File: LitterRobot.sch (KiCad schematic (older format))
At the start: 1 part, among them J1 Conn_02x02_Odd_Even

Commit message: Added Hirose footprints
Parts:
- removed J1: Conn_02x02_Odd_Even, LitterRobot:Hirose_DF11C-4DP-2V(57), symbol Connector_Generic:Conn_02x02_Odd_Even
- added J1: DF11C-4DP-2V(57), LitterRobot:Hirose_DF11C-4DP-2V(57), symbol Connector_Generic_MountingPin:Conn_02x02_Odd_Even_MountingPin
- added J2: Hirose_DF11C-6DP-2V(57), LitterRobot:Hirose_DF11C-6DP-2V(57), symbol Connector_Generic_MountingPin:Conn_02x03_Odd_Even_MountingPin
- added J3: DF11C-8DP-2V(57), LitterRobot:Hirose_DF11C-8DP-2V(57), symbol Connector_Generic_MountingPin:Conn_02x04_Odd_Even_MountingPin
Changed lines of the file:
@@
 encoding utf-8
 Sheet 1 1
-Title "Litter robot 3 - Main board"
+Title "Litter Robot 3 - Main board"
 Date "2021-02-27"
 Rev "A1"
@@
 $EndDescr
 $Comp
-L Connector_Generic:Conn_02x02_Odd_Even J1
-U 1 1 603B33C5
-P 2000 2050
-F 0 "J1" H 2050 2267 50  0000 C CNN
-F 1 "Conn_02x02_Odd_Even" H 2050 2176 50  0000 C CNN
-F 2 "LitterRobot:Hirose_DF11C-4DP-2V(57)" H 2000 2050 50  0001 C CNN
-F 3 "https://www.hirose.com/en/product/document?clcode=CL0543-0682-1-57&productname=DF11C-4DP-2V(57)&series=DF11&documenttype=2DDrawing&lang=en&documentid=0000926110" H 2000 2050 50  0001 C CNN
-	1    2000 2050
+L Connector_Generic_MountingPin:Conn_02x02_Odd_Even_MountingPin J1
+U 1 1 603B9D61
+P 2050 1550
+F 0 "J1" H 2100 1767 50  0000 C CNN
+F 1 "DF11C-4DP-2V(57)" H 2100 1676 50  0000 C CNN
+F 2 "LitterRobot:Hirose_DF11C-4DP-2V(57)" H 2050 1550 50  0001 C CNN
+F 3 "https://www.hirose.com/en/product/document?clcode=CL0543-0682-1-57&productname=DF11C-4DP-2V(57)&series=DF11&documenttype=2DDrawing&lang=en&documentid=0000926110" H 2050 1550 50  0001 C CNN
+	1    2050 1550
 	1    0    0    -1
 $EndComp
+$Comp
+L Connector_Generic_MountingPin:Conn_02x03_Odd_Even_MountingPin J2
+U 1 1 603BB210
+P 2050 2650
+F 0 "J2" H 2100 2967 50  0000 C CNN
+F 1 "Hirose_DF11C-6DP-2V(57)" H 2100 2876 50  0000 C CNN
+F 2 "LitterRobot:Hirose_DF11C-6DP-2V(57)" H 2050 2650 50  0001 C CNN
+F 3 "https://www.hirose.com/en/product/document?clcode=CL0543-0683-4-57&productname=DF11C-6DP-2V(57)&series=DF11&documenttype=2DDrawing&lang=en&documentid=0000926113" H 2050 2650 50  0001 C CNN
+	1    2050 2650
+	1    0    0    -1
+$EndComp
+$Comp
+L Connector_Generic_MountingPin:Conn_02x04_Odd_Even_MountingPin J3
+U 1 1 603BC30E
+P 2050 3650
+F 0 "J3" H 2100 3967 50  0000 C CNN
+F 1 "DF11C-8DP-2V(57)" H 2100 3876 50  0000 C CNN
+F 2 "LitterRobot:Hirose_DF11C-8DP-2V(57)" H 2050 3650 50  0001 C CNN
+F 3 "https://www.hirose.com/en/product/document?clcode=CL0543-0684-7-57&productname=DF11C-8DP-2V(57)&series=DF11&documenttype=2DDrawing&lang=en&documentid=0000999153" H 2050 3650 50  0001 C CNN
+	1    2050 3650
+	1    0    0    -1
+$EndComp

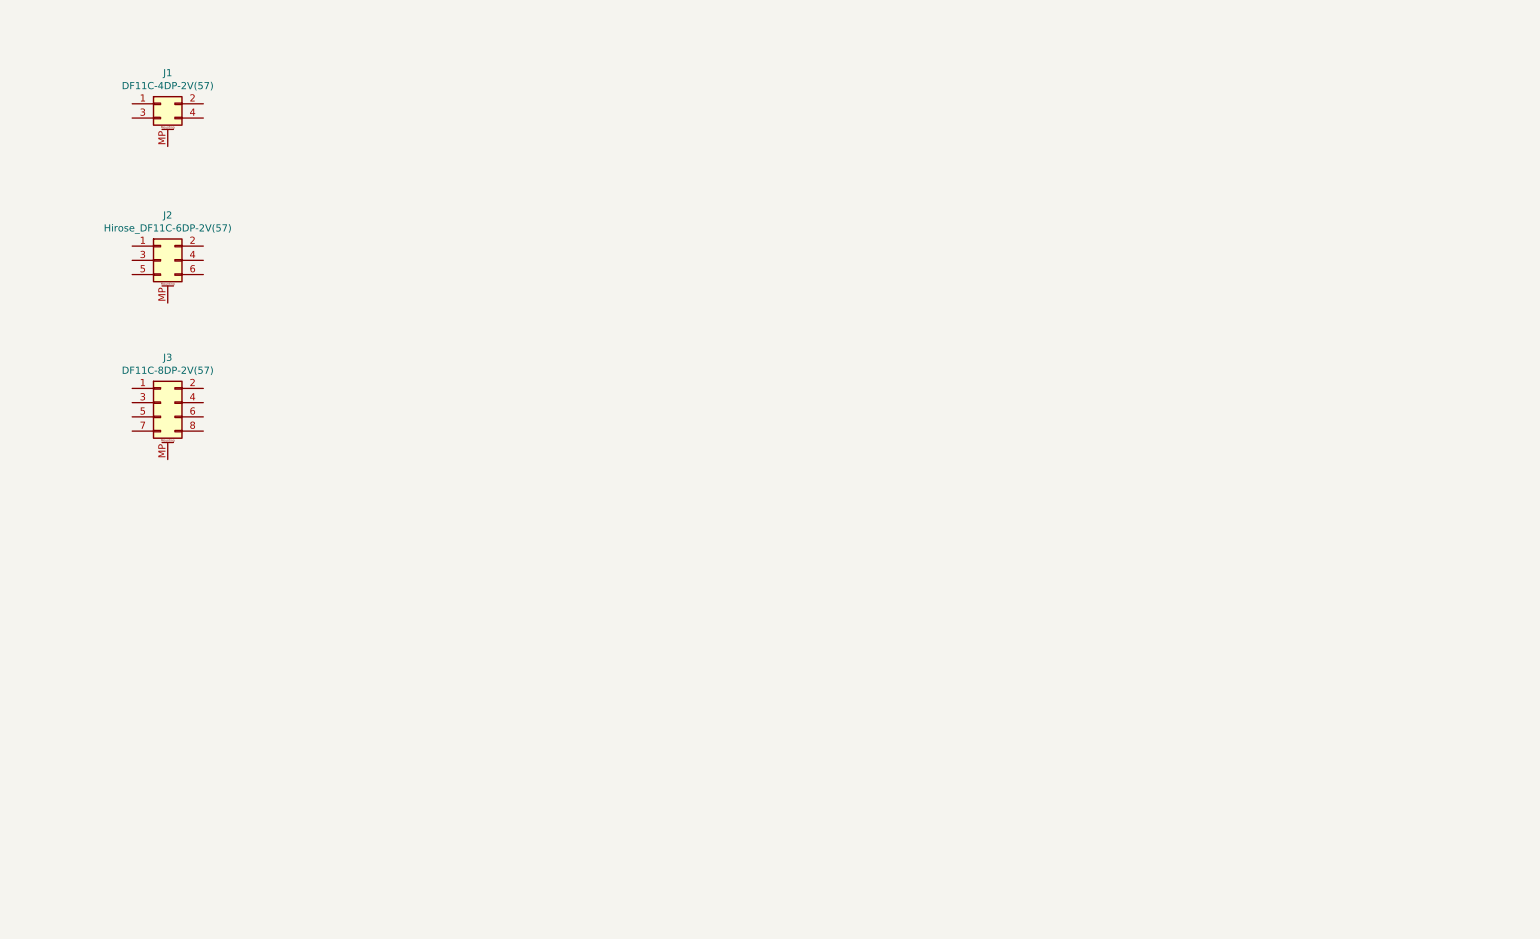
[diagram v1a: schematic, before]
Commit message: Add RGB LEDs to the schematic
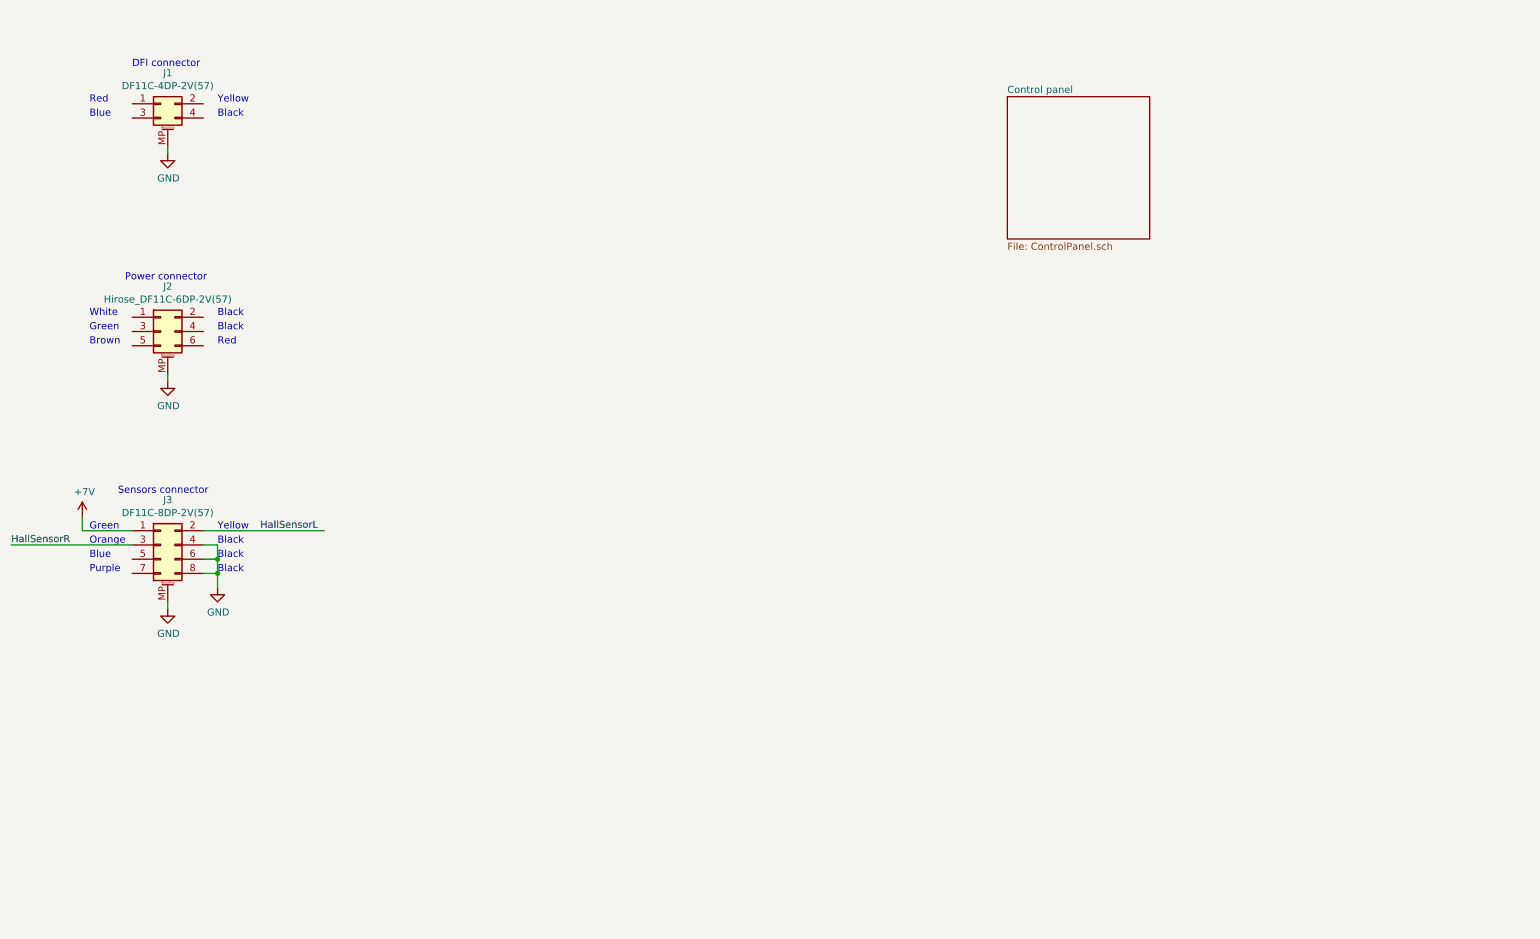
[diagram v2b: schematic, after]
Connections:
- net labels added: +7V, GND, HallSensorL, HallSensorR
- wire segments 0 -> 13
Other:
- note added: "Black"
- note added: "Blue"
- note added: "Brown"
- note added: "DFI connector"
- note added: "Green"
- note added: "Orange"
- note added: "Power connector"
- note added: "Purple"
- note added: "Red"
- note added: "Sensors connector"
- note added: "White"
- note added: "Yellow"
- moved on the sheet: J2, J3
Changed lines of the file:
@@
 $Descr A4 11693 8268
 encoding utf-8
-Sheet 1 1
+Sheet 1 13
 Title "Litter Robot 3 - Main board"
 Date "2021-02-27"
@@
 Comment4 ""
 $EndDescr
+$Comp
+L Connector_Generic_MountingPin:Conn_02x03_Odd_Even_MountingPin J2
+U 1 1 603BB210
+P 2050 3150
+F 0 "J2" H 2100 3467 50  0000 C CNN
+F 1 "Hirose_DF11C-6DP-2V(57)" H 2100 3376 50  0000 C CNN
+F 2 "LitterRobot:Hirose_DF11C-6DP-2V(57)" H 2050 3150 50  0001 C CNN
+F 3 "https://www.hirose.com/en/product/document?clcode=CL0543-0683-4-57&productname=DF11C-6DP-2V(57)&series=DF11&documenttype=2DDrawing&lang=en&documentid=0000926113" H 2050 3150 50  0001 C CNN
+	1    2050 3150
+	1    0    0    -1
+$EndComp
+$Comp
+L Connector_Generic_MountingPin:Conn_02x04_Odd_Even_MountingPin J3
+U 1 1 603BC30E
+P 2050 4650
+F 0 "J3" H 2100 4967 50  0000 C CNN
+F 1 "DF11C-8DP-2V(57)" H 2100 4876 50  0000 C CNN
+F 2 "LitterRobot:Hirose_DF11C-8DP-2V(57)" H 2050 4650 50  0001 C CNN
+F 3 "https://www.hirose.com/en/product/document?clcode=CL0543-0684-7-57&productname=DF11C-8DP-2V(57)&series=DF11&documenttype=2DDrawing&lang=en&documentid=0000999153" H 2050 4650 50  0001 C CNN
+	1    2050 4650
+	1    0    0    -1
+$EndComp
+Wire Wire Line
+	2100 1850 2100 1900
+$Comp
+L power:GND #PWR0101
+U 1 1 603BD2EA
+P 2100 1900
+F 0 "#PWR0101" H 2100 1650 50  0001 C CNN
+F 1 "GND" H 2105 1727 50  0000 C CNN
+F 2 "" H 2100 1900 50  0001 C CNN
+F 3 "" H 2100 1900 50  0001 C CNN
+	1    2100 1900
+	1    0    0    -1
+$EndComp
 $Comp
 L Connector_Generic_MountingPin:Conn_02x02_Odd_Even_MountingPin J1
@@
 	1    0    0    -1
 $EndComp
+Wire Wire Line
+	2100 3450 2100 3500
 $Comp
-L Connector_Generic_MountingPin:Conn_02x03_Odd_Even_MountingPin J2
-U 1 1 603BB210
-P 2050 2650
-F 0 "J2" H 2100 2967 50  0000 C CNN
-F 1 "Hirose_DF11C-6DP-2V(57)" H 2100 2876 50  0000 C CNN
-F 2 "LitterRobot:Hirose_DF11C-6DP-2V(57)" H 2050 2650 50  0001 C CNN
-F 3 "https://www.hirose.com/en/product/document?clcode=CL0543-0683-4-57&productname=DF11C-6DP-2V(57)&series=DF11&documenttype=2DDrawing&lang=en&documentid=0000926113" H 2050 2650 50  0001 C CNN
-	1    2050 2650
+L power:GND #PWR0102
+U 1 1 603C0906
+P 2100 3500
+F 0 "#PWR0102" H 2100 3250 50  0001 C CNN
+F 1 "GND" H 2105 3327 50  0000 C CNN
+F 2 "" H 2100 3500 50  0001 C CNN
+F 3 "" H 2100 3500 50  0001 C CNN
+	1    2100 3500
 	1    0    0    -1
 $EndComp
+Wire Wire Line
+	2100 5050 2100 5100
 $Comp
-L Connector_Generic_MountingPin:Conn_02x04_Odd_Even_MountingPin J3
-U 1 1 603BC30E
-P 2050 3650
-F 0 "J3" H 2100 3967 50  0000 C CNN
-F 1 "DF11C-8DP-2V(57)" H 2100 3876 50  0000 C CNN
-F 2 "LitterRobot:Hirose_DF11C-8DP-2V(57)" H 2050 3650 50  0001 C CNN
-F 3 "https://www.hirose.com/en/product/document?clcode=CL0543-0684-7-57&productname=DF11C-8DP-2V(57)&series=DF11&documenttype=2DDrawing&lang=en&documentid=0000999153" H 2050 3650 50  0001 C CNN
-	1    2050 3650
+L power:GND #PWR0103
+U 1 1 603C0C1B
+P 2100 5100
+F 0 "#PWR0103" H 2100 4850 50  0001 C CNN
+F 1 "GND" H 2105 4927 50  0000 C CNN
+F 2 "" H 2100 5100 50  0001 C CNN
+F 3 "" H 2100 5100 50  0001 C CNN
+	1    2100 5100
 	1    0    0    -1
 $EndComp
+Text Notes 1550 1550 0    50   ~ 0
+Red
+Text Notes 1550 1650 0    50   ~ 0
+Blue
+Text Notes 2450 1550 0    50   ~ 0
+Yellow
+Text Notes 2450 1650 0    50   ~ 0
+Black
+Text Notes 1850 1300 0    50   ~ 0
+DFI connector
+Text Notes 1800 2800 0    50   ~ 0
+Power connector
+Text Notes 1550 3050 0    50   ~ 0
+White
+Text Notes 1550 3150 0    50   ~ 0
+Green
+Text Notes 1550 3250 0    50   ~ 0
+Brown
+Text Notes 1750 4300 0    50   ~ 0
+Sensors connector
+Text Notes 1550 4550 0    50   ~ 0
+Green
+Text Notes 1550 4650 0    50   ~ 0
+Orange
+Text Notes 2450 4550 0    50   ~ 0
+Yellow
+Text Notes 1550 4750 0    50   ~ 0
+Blue
+Text Notes 1550 4850 0    50   ~ 0
+Purple
+Text Notes 2450 4650 0    50   ~ 0
+Black
+Text Notes 2450 4750 0    50   ~ 0
+Black
+Text Notes 2450 4850 0    50   ~ 0
+Black
+$Comp
+L power:GND #PWR0104
+U 1 1 603D1C90
+P 2450 4950
+F 0 "#PWR0104" H 2450 4700 50  0001 C CNN
+F 1 "GND" H 2455 4777 50  0000 C CNN
+F 2 "" H 2450 4950 50  0001 C CNN
+F 3 "" H 2450 4950 50  0001 C CNN
+	1    2450 4950
+	1    0    0    -1
+$EndComp
+Wire Wire Line
+	2350 4650 2450 4650
+Wire Wire Line
+	2450 4650 2450 4750
+Wire Wire Line
+	2350 4750 2450 4750
+Connection ~ 2450 4750
+Wire Wire Line
+	2450 4750 2450 4850
+Wire Wire Line
+	2350 4850 2450 4850
+Connection ~ 2450 4850
+Wire Wire Line
+	2450 4850 2450 4950
+Text Notes 2450 3250 0    50   ~ 0
+Red
+Text Notes 2450 3050 0    50   ~ 0
+Black
+Text Notes 2450 3150 0    50   ~ 0
+Black
+Wire Wire Line
+	1850 4650 1000 4650
+Text Label 1000 4650 0    50   ~ 0
+HallSensorR
+Wire Wire Line
+	3200 4550 2350 4550
+Text Label 2750 4550 0    50   ~ 0
+HallSensorL
+Wire Wire Line
+	1850 4550 1500 4550
+Wire Wire Line
+	1500 4550 1500 4450
+$Sheet
+S 8000 1500 1000 1000
+U 603E03AA
+F0 "Control panel" 50
+F1 "ControlPanel.sch" 50
+$EndSheet
+$Comp
+L LitterRobot:+7V #PWR?
+U 1 1 60414DA6
+P 1500 4450
+F 0 "#PWR?" H 1500 4300 50  0001 C CNN
+F 1 "+7V" H 1515 4623 50  0000 C CNN
+F 2 "" H 1500 4450 50  0001 C CNN
+F 3 "" H 1500 4450 50  0001 C CNN
+	1    1500 4450
+	1    0    0    -1
+$EndComp

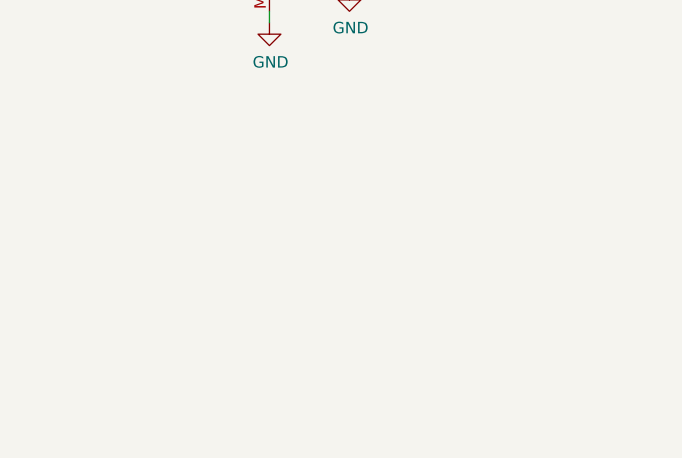
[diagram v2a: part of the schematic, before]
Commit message: Add an extension connector
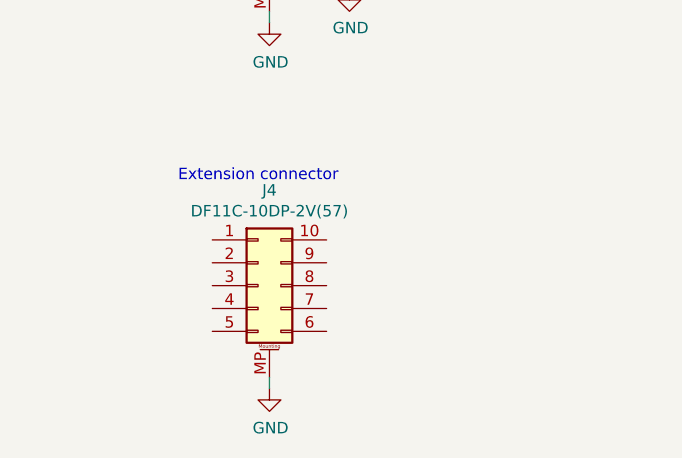
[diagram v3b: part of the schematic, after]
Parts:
- added J4: DF11C-10DP-2V(57), LitterRobot:Hirose_DF11C-10DP-2V(57), symbol Connector_Generic_MountingPin:Conn_02x05_Counter_Clockwise_MountingPin
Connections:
- wire segments 13 -> 14
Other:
- note added: "Extension connector"
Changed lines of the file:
@@
 	1    0    0    -1
 $EndComp
+$Comp
+L Connector_Generic_MountingPin:Conn_02x05_Counter_Clockwise_MountingPin J4
+U 1 1 603E9ABF
+P 2050 6250
+F 0 "J4" H 2100 6667 50  0000 C CNN
+F 1 "DF11C-10DP-2V(57)" H 2100 6576 50  0000 C CNN
+F 2 "LitterRobot:Hirose_DF11C-10DP-2V(57)" H 2050 6250 50  0001 C CNN
+F 3 "~" H 2050 6250 50  0001 C CNN
+	1    2050 6250
+	1    0    0    -1
+$EndComp
+Wire Wire Line
+	2100 6650 2100 6700
+$Comp
+L power:GND #PWR?
+U 1 1 603F0326
+P 2100 6700
+F 0 "#PWR?" H 2100 6450 50  0001 C CNN
+F 1 "GND" H 2105 6527 50  0000 C CNN
+F 2 "" H 2100 6700 50  0001 C CNN
+F 3 "" H 2100 6700 50  0001 C CNN
+	1    2100 6700
+	1    0    0    -1
+$EndComp
+Text Notes 1700 5800 0    50   ~ 0
+Extension connector
 $EndSCHEMATC

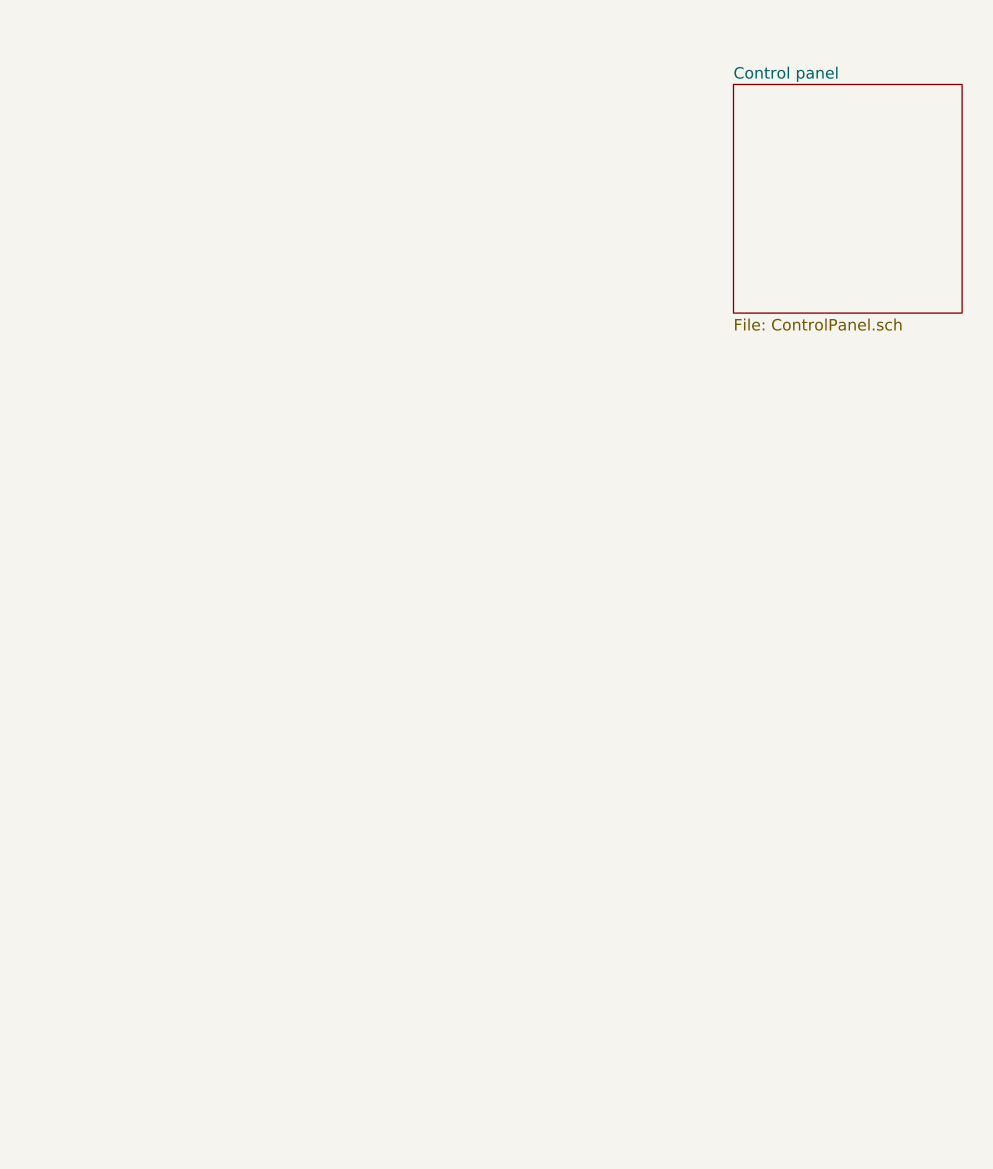
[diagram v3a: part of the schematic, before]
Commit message: Add placeholder sheets for functions to be implemented
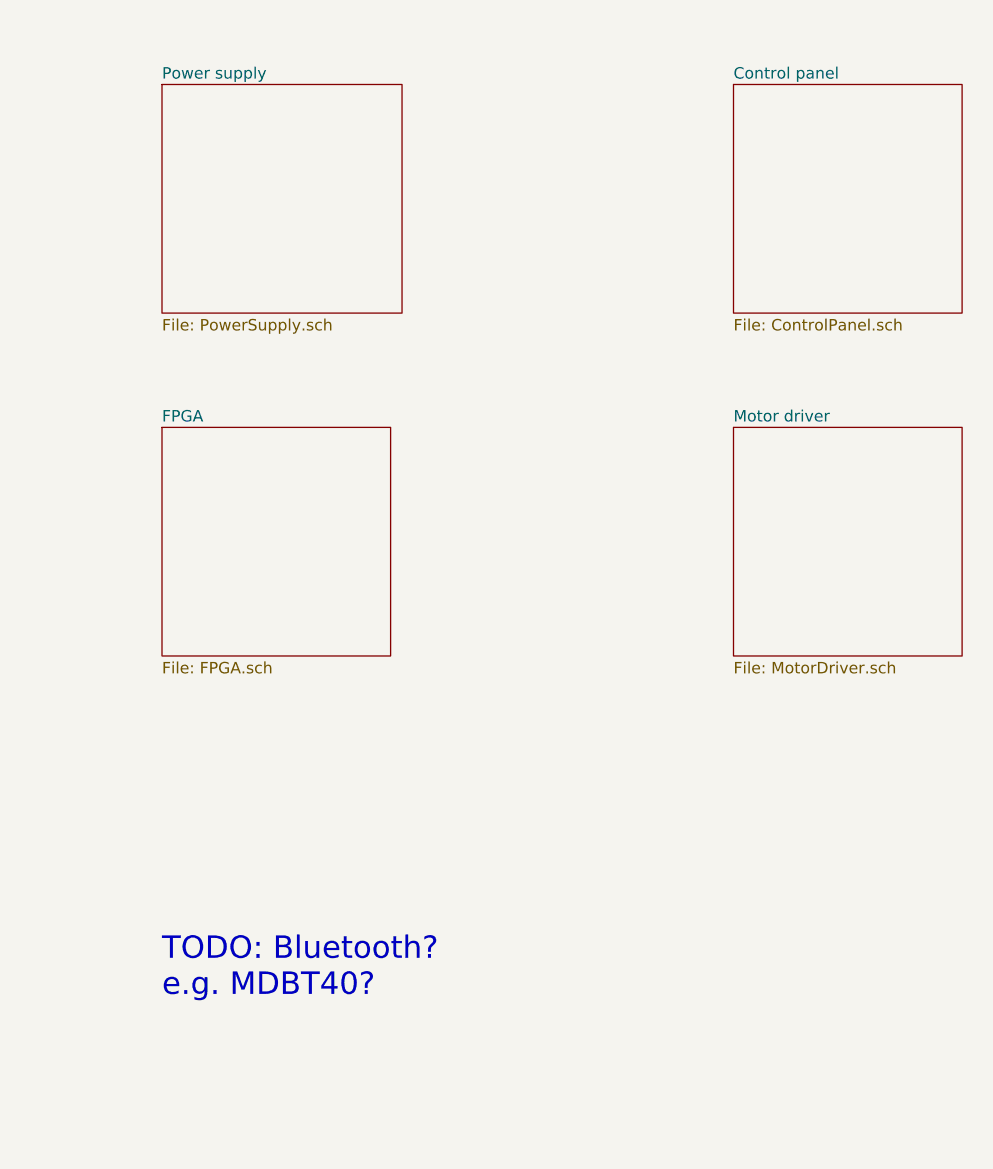
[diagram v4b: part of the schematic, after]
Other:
- note added: "TODO: Bluetooth?\ne.g. MDBT40?"
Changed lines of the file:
@@
 $Descr A4 11693 8268
 encoding utf-8
-Sheet 1 13
+Sheet 1 16
 Title "Litter Robot 3 - Main board"
 Date "2021-02-27"
@@
 Text Notes 1700 5800 0    50   ~ 0
 Extension connector
+$Sheet
+S 5500 1500 1050 1000
+U 603F1DCE
+F0 "Power supply" 50
+F1 "PowerSupply.sch" 50
+$EndSheet
+$Sheet
+S 5500 3000 1000 1000
+U 603F1F4D
+F0 "FPGA" 50
+F1 "FPGA.sch" 50
+$EndSheet
+$Sheet
+S 8000 3000 1000 1000
+U 603F20AB
+F0 "Motor driver" 50
+F1 "MotorDriver.sch" 50
+$EndSheet
+Text Notes 5500 5500 0    98   ~ 0
+TODO: Bluetooth?\ne.g. MDBT40?
 $EndSCHEMATC
